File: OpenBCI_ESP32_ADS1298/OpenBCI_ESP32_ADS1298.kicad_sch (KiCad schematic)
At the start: 1 part

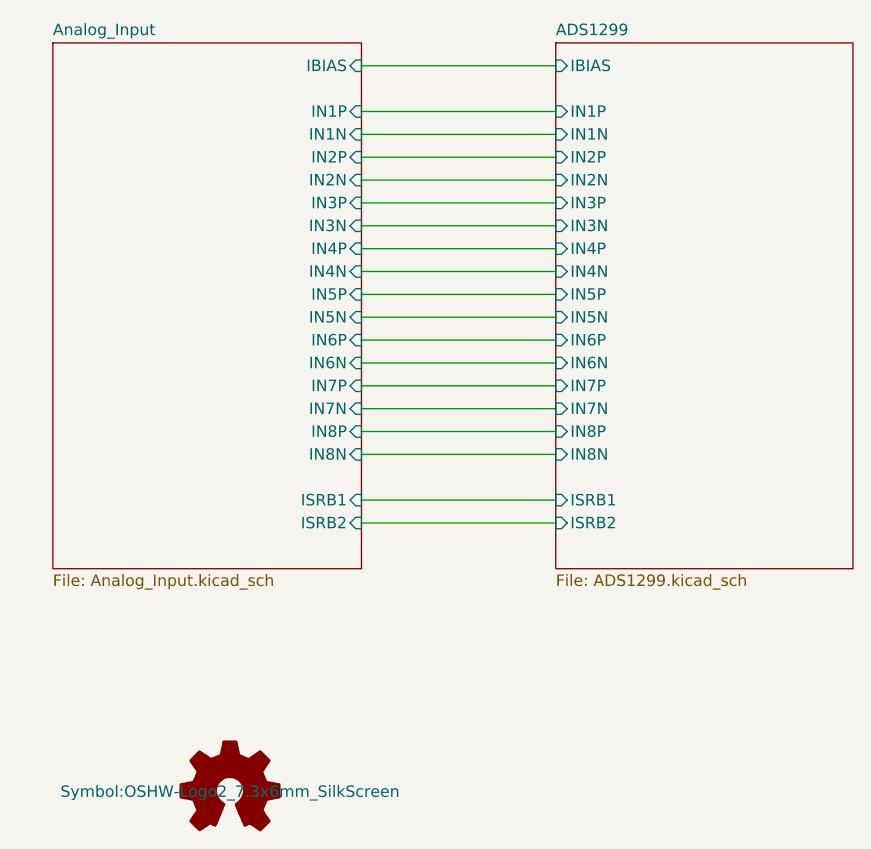
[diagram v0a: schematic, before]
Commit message: add ADS1298 files
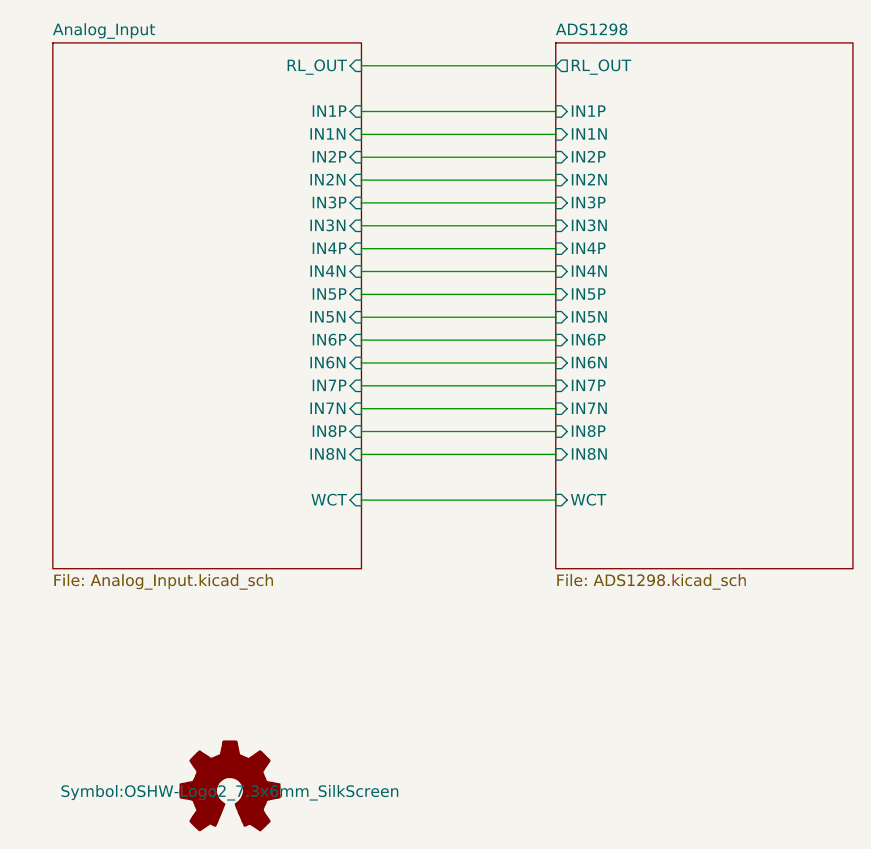
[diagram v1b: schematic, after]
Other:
- sheet ADS1299 renamed ADS1298
- sheet ADS1298: file ADS1299.kicad_sch -> ADS1298.kicad_sch
- sheet ADS1298 ports: added RL_OUT, WCT; removed IBIAS, ISRB1, ISRB2
- sheet Analog_Input ports: added RL_OUT, WCT; removed IBIAS, ISRB1, ISRB2
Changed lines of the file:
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@@
+    (stroke (width 0) (type default))
+  )
+  (wire (pts (xy 113.03 64.77) (xy 134.62 64.77))
+    (stroke (width 0) (type default))
+  )
+  (wire (pts (xy 113.03 82.55) (xy 134.62 82.55))
+    (stroke (width 0) (type default))
+  )
+  (wire (pts (xy 113.03 39.37) (xy 134.62 39.37))
+    (stroke (width 0) (type default))
+  )
+  (wire (pts (xy 113.03 46.99) (xy 134.62 46.99))
     (stroke (width 0) (type default))
   )
@@
     (stroke (width 0) (type default))
   )
-  (wire (pts (xy 113.03 64.77) (xy 134.62 64.77))
-    (stroke (width 0) (type default))
-  )
-  (wire (pts (xy 134.62 85.09) (xy 113.03 85.09))
-    (stroke (width 0) (type default))
-  )
-  (wire (pts (xy 113.03 39.37) (xy 134.62 39.37))
-    (stroke (width 0) (type default))
-  )
-  (wire (pts (xy 113.03 46.99) (xy 134.62 46.99))
-    (stroke (width 0) (type default))
-  )
   (wire (pts (xy 113.03 62.23) (xy 134.62 62.23))
     (stroke (width 0) (type default))
@@
   )
   (wire (pts (xy 113.03 52.07) (xy 134.62 52.07))
-    (stroke (width 0) (type default))
-  )
-  (wire (pts (xy 113.03 82.55) (xy 134.62 82.55))
     (stroke (width 0) (type default))
   )
@@
     )
     (instances
-      (project "OpenBCI_ESP32_INPUT"
+      (project "OpenBCI_ESP32_ADS1298"
         (path "/c05ecaff-48cd-4ff1-bf9c-1e68fad43fda"
           (reference "LOGO1") (unit 1)
@@
       (effects (font (size 1.27 1.27)) (justify right))
     )
-    (pin "IBIAS" input (at 113.03 34.29 0)
-      (effects (font (size 1.27 1.27)) (justify right))
-    )
-    (pin "ISRB1" input (at 113.03 82.55 0)
-      (effects (font (size 1.27 1.27)) (justify right))
-    )
-    (pin "ISRB2" input (at 113.03 85.09 0)
+    (pin "RL_OUT" input (at 113.03 34.29 0)
+      (effects (font (size 1.27 1.27)) (justify right))
+    )
+    (pin "WCT" input (at 113.03 82.55 0)
       (effects (font (size 1.27 1.27)) (justify right))
     )
     (instances
-      (project "OpenBCI_ESP32_INPUT"
+      (project "OpenBCI_ESP32_ADS1298"
         (path "/c05ecaff-48cd-4ff1-bf9c-1e68fad43fda" (page "3"))
       )
@@
     (stroke (width 0) (type solid))
     (fill (color 0 0 0 0.0000))
-    (property "Sheetname" "ADS1299" (at 134.62 31.0384 0)
+    (property "Sheetname" "ADS1298" (at 134.62 31.0384 0)
       (effects (font (size 1.27 1.27)) (justify left bottom))
     )
-    (property "Sheetfile" "ADS1299.kicad_sch" (at 134.62 90.7546 0)
+    (property "Sheetfile" "ADS1298.kicad_sch" (at 134.62 90.7546 0)
       (effects (font (size 1.27 1.27)) (justify left top))
     )
@@
       (effects (font (size 1.27 1.27)) (justify left))
     )
-    (pin "IBIAS" input (at 134.62 34.29 180)
-      (effects (font (size 1.27 1.27)) (justify left))
-    )
-    (pin "ISRB1" input (at 134.62 82.55 180)
-      (effects (font (size 1.27 1.27)) (justify left))
-    )
-    (pin "ISRB2" input (at 134.62 85.09 180)
+    (pin "WCT" input (at 134.62 82.55 180)
+      (effects (font (size 1.27 1.27)) (justify left))
+    )
+    (pin "RL_OUT" output (at 134.62 34.29 180)
       (effects (font (size 1.27 1.27)) (justify left))
     )
     (instances
-      (project "OpenBCI_ESP32_INPUT"
+      (project "OpenBCI_ESP32_ADS1298"
         (path "/c05ecaff-48cd-4ff1-bf9c-1e68fad43fda" (page "2"))
       )
